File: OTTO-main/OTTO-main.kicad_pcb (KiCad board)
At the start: 4 copper layers, 247 x 81 mm, 142 parts, among them J1 POWER_BOARD, J2 AUDIO_BOARD, J3 Raspberry_Pi_2_3, J4 MICROPHONE, J5 Conn_01x24, SW1 SW_SPST, SW10 SW_SPST, SW11 SW_SPST, SW12 SW_SPST, SW13 Rotary_Encoder_Switch, SW14 Rotary_Encoder_Switch, SW15 SW_SPST, SW16 SW_SPST, SW17 SW_SPST, SW18 SW_SPST, SW19 SW_SPST, SW2 SW_SPST, SW20 SW_SPST, SW21 SW_SPST, SW22 SW_SPST, SW23 SW_SPST, SW24 SW_SPST, SW25 SW_SPST, SW26 SW_SPST, SW27 Rotary_Encoder_Switch, SW28 Rotary_Encoder_Switch, SW29 SW_SPST, SW3 SW_SPST, SW30 SW_SPST, SW31 SW_SPST, SW32 SW_SPST, SW33 SW_SPST, SW34 SW_SPST, SW35 SW_SPST, SW36 SW_SPST, SW37 SW_SPST, SW38 SW_SPST, SW39 SW_SPST, SW4 SW_SPST, SW40 SW_SPST, SW41 SW_SPST, SW42 SW_SPST, SW5 SW_SPST, SW6 SW_SPST, SW7 SW_SPST, SW8 SW_SPST, SW9 SW_SPST, U1 STM32F103RETx, U2 74AHCT1G125, U3 ILI9341, Y1 8mhz

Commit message: re-wired the stm32 to optimize the routing
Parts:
- moved L1 39.8 mm to (193.9, 74.2), turned to 45 degrees
- moved C7 35.8 mm to (191.8, 72.1), turned to 45 degrees
- moved C5 35.4 mm to (183.7, 57.3), turned to 315 degrees
- moved C9 33.4 mm to (190.0, 79.4), turned to 315 degrees
- moved C6 32.1 mm to (189.7, 69.9), turned to 45 degrees
- moved C8 30.8 mm to (187.9, 81.6), turned to 315 degrees
- moved C3 26.1 mm to (177.4, 76.4), turned to 135 degrees
- moved Y1 24.2 mm to (185.4, 77.0), turned to 45 degrees
- moved C4 24.1 mm to (189.3, 62.7), turned to 315 degrees
- moved U1 22.1 mm to (180.3, 66.7), turned to 135 degrees
- moved J5 2.00 mm to (258.6, 115.2)
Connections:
- J5 pad 1: ROW4 -> COL1
- J5 pad 10: COL8 -> COL10
- J5 pad 11: COL9 -> COL11
- J5 pad 12: COL10 -> COL12
- J5 pad 13: COL11 -> COL13
- J5 pad 14: COL12 -> COL14
- J5 pad 15: COL13 -> (no net)
- J5 pad 16: COL14 -> (no net)
- J5 pad 2: ROW5 -> COL2
- J5 pad 3: COL1 -> COL3
- J5 pad 4: COL2 -> COL4
- J5 pad 5: COL3 -> COL5
- J5 pad 6: COL4 -> COL6
- J5 pad 7: COL5 -> COL7
- J5 pad 8: COL6 -> COL8
- J5 pad 9: COL7 -> COL9
- U1 pad 10: COL3 -> (no net)
- U1 pad 11: COL4 -> (no net)
- U1 pad 14: COL5 -> (no net)
- U1 pad 15: COL6 -> (no net)
- U1 pad 16: COL7 -> (no net)
- U1 pad 17: COL8 -> (no net)
- U1 pad 2: (no net) -> COL11
- U1 pad 20: COL9 -> (no net)
- U1 pad 21: COL10 -> (no net)
- U1 pad 22: COL11 -> (no net)
- U1 pad 23: COL12 -> (no net)
- U1 pad 24: COL13 -> (no net)
- U1 pad 25: COL14 -> (no net)
- U1 pad 26: ROW1 -> (no net)
- U1 pad 27: ROW2 -> (no net)
- U1 pad 29: ROW3 -> (no net)
- U1 pad 3: (no net) -> COL12
- U1 pad 33: (no net) -> ENC1_B
- U1 pad 34: ENC4_A -> ENC1_A
- U1 pad 35: ENC4_B -> ENC2_B
- U1 pad 36: ENC3_A -> ENC2_A
- U1 pad 38: ENC2_A -> ENC3_A
- U1 pad 39: ENC2_B -> ENC4_B
- U1 pad 4: (no net) -> COL13
- U1 pad 40: ENC1_A -> ENC4_A
- U1 pad 41: ENC1_B -> LEDIN
- U1 pad 44: LEDIN -> ROW1
- U1 pad 45: (no net) -> ROW2
- U1 pad 46: (no net) -> ROW3
- U1 pad 49: ROW4 -> COL1
- U1 pad 50: ROW5 -> COL2
- U1 pad 51: (no net) -> COL3
- U1 pad 52: (no net) -> COL4
- U1 pad 53: (no net) -> COL5
- U1 pad 55: (no net) -> COL6
- U1 pad 56: (no net) -> COL7
- U1 pad 57: (no net) -> COL8
- U1 pad 61: (no net) -> COL9
- U1 pad 62: (no net) -> COL10
- U1 pad 8: COL1 -> COL14
- U1 pad 9: COL2 -> (no net)
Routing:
- net ROW5: track 120.5 -> 0.00 mm, vias 4 -> 0
- net ROW4: track 117.8 -> 0.00 mm, vias 4 -> 0
- net ROW1: track 413.6 -> 329.3 mm, vias 8 -> 7
- net ROW3: track 307.1 -> 345.6 mm
- net COL12: track 217.7 -> 190.9 mm, vias 6 -> 4
- net COL10: track 276.3 -> 253.5 mm, vias 6 -> 4
- net COL11: track 161.9 -> 139.3 mm
- net COL8: track 173.0 -> 191.2 mm, vias 4 -> 2
- net ENC1_A: track 155.1 -> 140.2 mm, vias 2 -> 0
- net ENC1_B: track 159.4 -> 145.3 mm, vias 2 -> 0
- net ENC2_A: track 122.9 -> 109.0 mm, vias 2 -> 0
- net ENC2_B: track 127.2 -> 114.1 mm, vias 2 -> 0
- net LEDIN: track 174.3 -> 161.4 mm, vias 3 -> 1
- net GND: track 187.6 -> 174.7 mm, vias 67 -> 63
- net ENC4_A: track 57.2 -> 44.5 mm, vias 2 -> 0
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
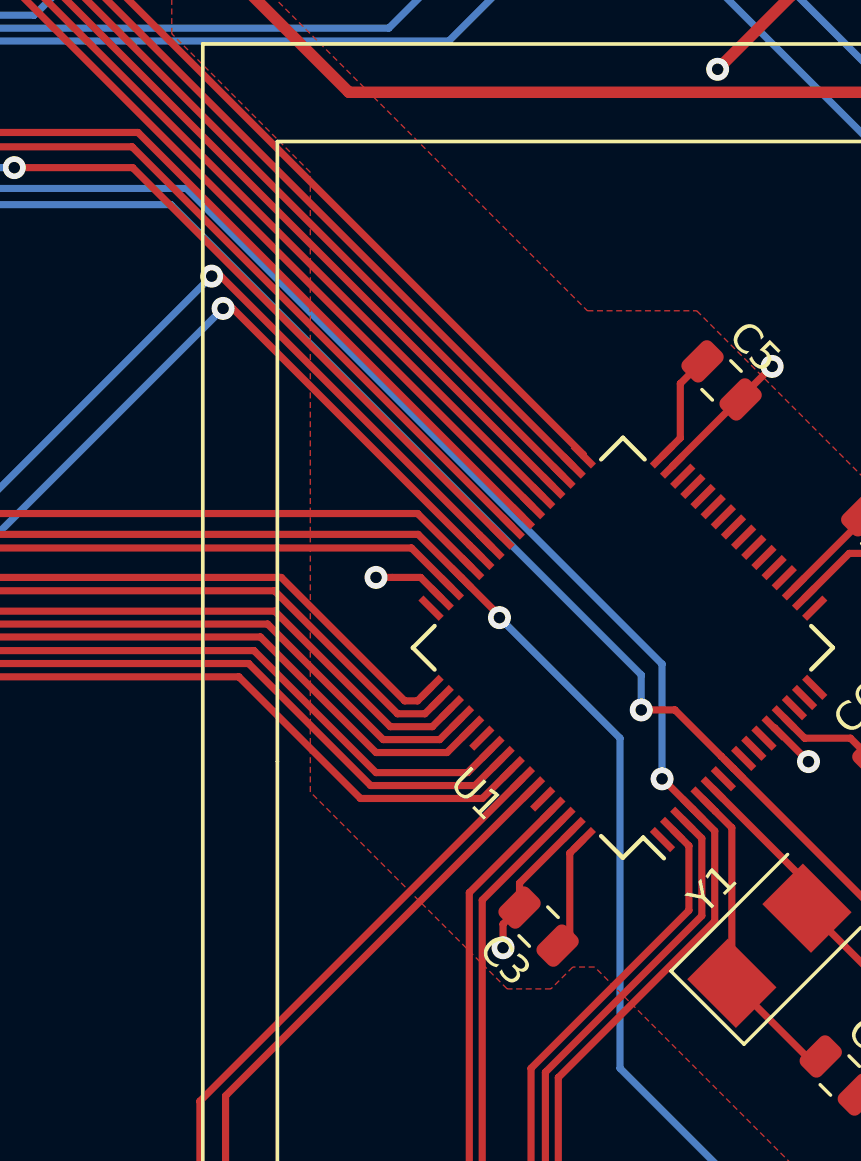
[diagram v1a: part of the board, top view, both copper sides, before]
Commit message: added the OTTO-Keys board and fixed some of the mainboard issues
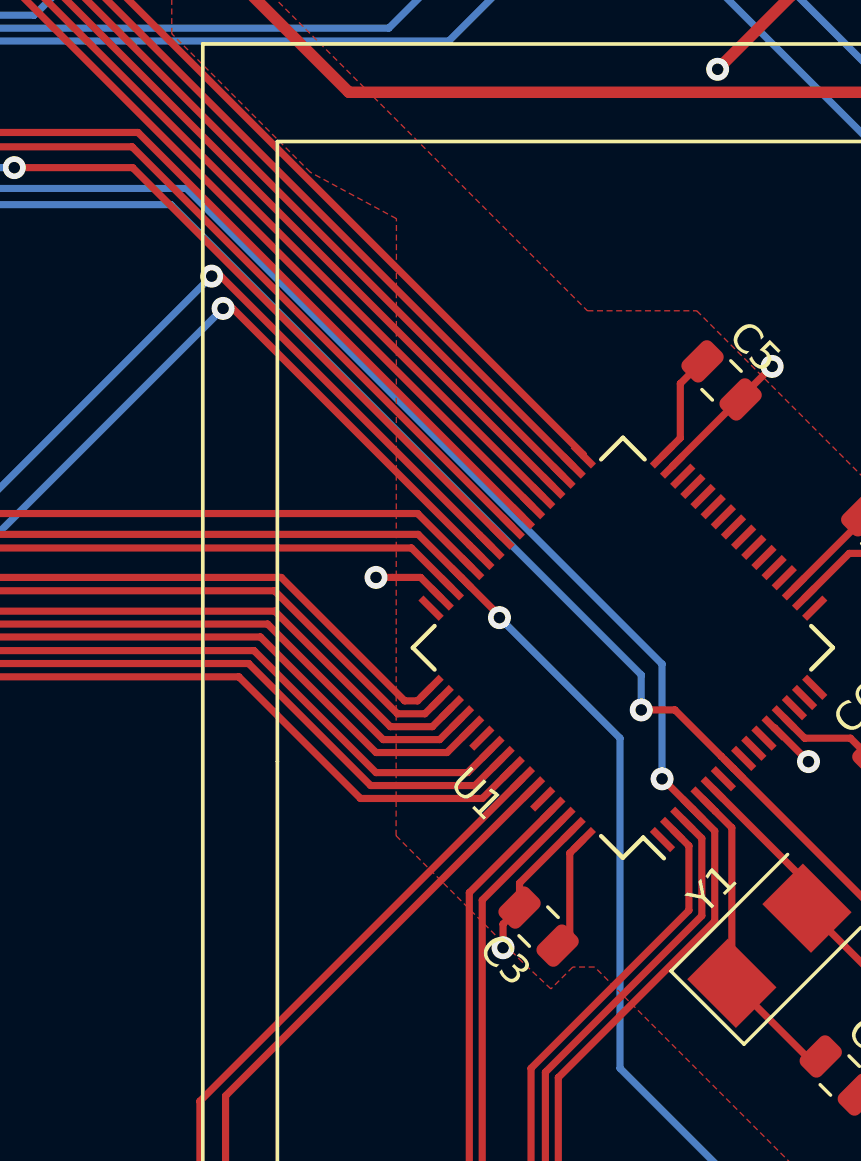
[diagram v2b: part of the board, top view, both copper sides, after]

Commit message: added the OTTO-keys files
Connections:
- J5 pad 15: (no net) -> ROW4
- J5 pad 16: (no net) -> ROW5
- U1 pad 10: (no net) -> ROW5
- U1 pad 9: (no net) -> ROW4
- U2 pad 1: GND -> (no net)
- U2 pad 5: 5V -> (no net)
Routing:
- net ROW5: track 0.00 -> 106.8 mm, vias 0 -> 4
- net ROW4: track 0.00 -> 104.7 mm, vias 0 -> 4
- net ROW1: track 329.3 -> 412.1 mm, vias 7 -> 11
- net GND: track 174.7 -> 197.3 mm, vias 63 -> 65
- net 5V: track 412.1 -> 433.8 mm, vias 79 -> 80
- net Net-(D50-Pad2): track 133.4 -> 123.5 mm
- net I2S_TX: track 207.8 -> 211.4 mm
- net I2S_RX: track 214.2 -> 216.6 mm
- net (no net): track 0.00 -> 1.76 mm, vias 0 -> 1
- net Net-(D58-Pad2): track 124.7 -> 126.3 mm
- net BCLK: track 179.0 -> 180.4 mm
- net COL14: track 235.1 -> 236.4 mm
- net SDA: track 250.5 -> 251.4 mm
- net COL1: track 393.2 -> 392.3 mm
- net 3V3: track 175.6 -> 174.8 mm
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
